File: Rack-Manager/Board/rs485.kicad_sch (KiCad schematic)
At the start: 28 parts, among them J5 Conn_01x03_Pin, J6 Conn_01x03_Pin, U8 THVD1450DRBR, U9 THVD1450DRBR

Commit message: Updated .gitignore, added USB-C sink controller and fix earth on GDT
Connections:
- net GND: no longer GD1.2, GD2.2
- new net Earth: GD1.2, GD2.2
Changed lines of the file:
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@@
+	)
+	(symbol
+		(lib_id "power:Earth")
+		(at 215.9 128.27 90)
+		(unit 1)
+		(exclude_from_sim no)
+		(in_bom yes)
+		(on_board yes)
+		(dnp no)
+		(property "Reference" "#PWR064"
+			(at 222.25 128.27 0)
+			(effects
+				(font
+					(size 1.27 1.27)
+				)
+				(hide yes)
+			)
+		)
+		(property "Value" "Earth"
+			(at 220.345 128.27 0)
+			(effects
+				(font
+					(size 1.27 1.27)
+				)
+			)
+		)
+		(property "Footprint" ""
+			(at 215.9 128.27 0)
+			(effects
+				(font
+					(size 1.27 1.27)
+				)
+				(hide yes)
+			)
+		)
+		(property "Datasheet" "~"
+			(at 215.9 128.27 0)
+			(effects
+				(font
+					(size 1.27 1.27)
+				)
+				(hide yes)
+			)
+		)
+		(property "Description" "Power symbol creates a global label with name \"Earth\""
+			(at 215.9 128.27 0)
+			(effects
+				(font
+					(size 1.27 1.27)
+				)
+				(hide yes)
+			)
+		)
+		(pin "1"
+		)
+		(instances
+			(project "Rack-Manager"
+				(path "/5d42174d-da49-4bca-870b-353868af7168/9f35d409-1fd7-4241-ba93-dffedac70e6f"
+					(reference "#PWR064")
+					(unit 1)
+				)
+			)
+		)
 	)
 	(symbol
@@
 	)
 	(symbol
-		(lib_id "power:GND")
+		(lib_id "power:Earth")
 		(at 215.9 55.88 90)
 		(unit 1)
@@
 		(on_board yes)
 		(dnp no)
-		(property "Reference" "#PWR045"
+		(property "Reference" "#PWR051"
 			(at 222.25 55.88 0)
 			(effects
@@
 			)
 		)
-		(property "Value" "GND"
-			(at 220.98 56.642 90)
+		(property "Value" "Earth"
+			(at 220.345 55.88 0)
 			(effects
 				(font
@@
 			)
 		)
-		(property "Datasheet" ""
+		(property "Datasheet" "~"
 			(at 215.9 55.88 0)
 			(effects
@@
 			)
 		)
-		(property "Description" "Power symbol creates a global label with name \"GND\" , ground"
+		(property "Description" "Power symbol creates a global label with name \"Earth\""
 			(at 215.9 55.88 0)
 			(effects
@@
 			(project "Rack-Manager"
 				(path "/5d42174d-da49-4bca-870b-353868af7168/9f35d409-1fd7-4241-ba93-dffedac70e6f"
-					(reference "#PWR045")
+					(reference "#PWR051")
 					(unit 1)
 				)
@@
 				(path "/5d42174d-da49-4bca-870b-353868af7168/9f35d409-1fd7-4241-ba93-dffedac70e6f"
 					(reference "#PWR070")
-					(unit 1)
-				)
-			)
-		)
-	)
-	(symbol
-		(lib_id "power:GND")
-		(at 195.58 128.27 90)
-		(unit 1)
-		(exclude_from_sim no)
-		(in_bom yes)
-		(on_board yes)
-		(dnp no)
-		(property "Reference" "#PWR039"
-			(at 201.93 128.27 0)
-			(effects
-				(font
-					(size 1.27 1.27)
-				)
-				(hide yes)
-			)
-		)
-		(property "Value" "GND"
-			(at 200.66 128.27 90)
-			(effects
-				(font
-					(size 1.27 1.27)
-				)
-			)
-		)
-		(property "Footprint" ""
-			(at 195.58 128.27 0)
-			(effects
-				(font
-					(size 1.27 1.27)
-				)
-				(hide yes)
-			)
-		)
-		(property "Datasheet" ""
-			(at 195.58 128.27 0)
-			(effects
-				(font
-					(size 1.27 1.27)
-				)
-				(hide yes)
-			)
-		)
-		(property "Description" "Power symbol creates a global label with name \"GND\" , ground"
-			(at 195.58 128.27 0)
-			(effects
-				(font
-					(size 1.27 1.27)
-				)
-				(hide yes)
-			)
-		)
-		(pin "1"
-		)
-		(instances
-			(project "Rack-Manager"
-				(path "/5d42174d-da49-4bca-870b-353868af7168/9f35d409-1fd7-4241-ba93-dffedac70e6f"
-					(reference "#PWR039")
 					(unit 1)
 				)
@@
 	)
 	(symbol
+		(lib_id "power:GND")
+		(at 195.58 55.88 90)
+		(unit 1)
+		(exclude_from_sim no)
+		(in_bom yes)
+		(on_board yes)
+		(dnp no)
+		(property "Reference" "#PWR045"
+			(at 201.93 55.88 0)
+			(effects
+				(font
+					(size 1.27 1.27)
+				)
+				(hide yes)
+			)
+		)
+		(property "Value" "GND"
+			(at 200.025 55.88 0)
+			(effects
+				(font
+					(size 1.27 1.27)
+				)
+			)
+		)
+		(property "Footprint" ""
+			(at 195.58 55.88 0)
+			(effects
+				(font
+					(size 1.27 1.27)
+				)
+				(hide yes)
+			)
+		)
+		(property "Datasheet" ""
+			(at 195.58 55.88 0)
+			(effects
+				(font
+					(size 1.27 1.27)
+				)
+				(hide yes)
+			)
+		)
+		(property "Description" "Power symbol creates a global label with name \"GND\" , ground"
+			(at 195.58 55.88 0)
+			(effects
+				(font
+					(size 1.27 1.27)
+				)
+				(hide yes)
+			)
+		)
+		(pin "1"
+		)
+		(instances
+			(project "Rack-Manager"
+				(path "/5d42174d-da49-4bca-870b-353868af7168/9f35d409-1fd7-4241-ba93-dffedac70e6f"
+					(reference "#PWR045")
+					(unit 1)
+				)
+			)
+		)
+	)
+	(symbol
 		(lib_id "Bourns:TBU-CA")
 		(at 196.85 39.37 0)
@@
 	)
 	(symbol
+		(lib_id "power:GND")
+		(at 195.58 128.27 90)
+		(unit 1)
+		(exclude_from_sim no)
+		(in_bom yes)
+		(on_board yes)
+		(dnp no)
+		(property "Reference" "#PWR039"
+			(at 201.93 128.27 0)
+			(effects
+				(font
+					(size 1.27 1.27)
+				)
+				(hide yes)
+			)
+		)
+		(property "Value" "GND"
+			(at 200.025 128.27 0)
+			(effects
+				(font
+					(size 1.27 1.27)
+				)
+			)
+		)
+		(property "Footprint" ""
+			(at 195.58 128.27 0)
+			(effects
+				(font
+					(size 1.27 1.27)
+				)
+				(hide yes)
+			)
+		)
+		(property "Datasheet" ""
+			(at 195.58 128.27 0)
+			(effects
+				(font
+					(size 1.27 1.27)
+				)
+				(hide yes)
+			)
+		)
+		(property "Description" "Power symbol creates a global label with name \"GND\" , ground"
+			(at 195.58 128.27 0)
+			(effects
+				(font
+					(size 1.27 1.27)
+				)
+				(hide yes)
+			)
+		)
+		(pin "1"
+		)
+		(instances
+			(project "Rack-Manager"
+				(path "/5d42174d-da49-4bca-870b-353868af7168/9f35d409-1fd7-4241-ba93-dffedac70e6f"
+					(reference "#PWR039")
+					(unit 1)
+				)
+			)
+		)
+	)
+	(symbol
 		(lib_id "Texas Instruments:THVD1450DRBR")
 		(at 127 119.38 0)
@@
 	)
 	(symbol
-		(lib_id "power:GND")
-		(at 195.58 55.88 90)
-		(unit 1)
-		(exclude_from_sim no)
-		(in_bom yes)
-		(on_board yes)
-		(dnp no)
-		(property "Reference" "#PWR051"
-			(at 201.93 55.88 0)
-			(effects
-				(font
-					(size 1.27 1.27)
-				)
-				(hide yes)
-			)
-		)
-		(property "Value" "GND"
-			(at 200.66 55.88 90)
-			(effects
-				(font
-					(size 1.27 1.27)
-				)
-			)
-		)
-		(property "Footprint" ""
-			(at 195.58 55.88 0)
-			(effects
-				(font
-					(size 1.27 1.27)
-				)
-				(hide yes)
-			)
-		)
-		(property "Datasheet" ""
-			(at 195.58 55.88 0)
-			(effects
-				(font
-					(size 1.27 1.27)
-				)
-				(hide yes)
-			)
-		)
-		(property "Description" "Power symbol creates a global label with name \"GND\" , ground"
-			(at 195.58 55.88 0)
-			(effects
-				(font
-					(size 1.27 1.27)
-				)
-				(hide yes)
-			)
-		)
-		(pin "1"
-		)
-		(instances
-			(project "Rack-Manager"
-				(path "/5d42174d-da49-4bca-870b-353868af7168/9f35d409-1fd7-4241-ba93-dffedac70e6f"
-					(reference "#PWR051")
-					(unit 1)
-				)
-			)
-		)
-	)
-	(symbol
 		(lib_id "Device:R_Small_US")
 		(at 167.64 62.23 90)
@@
 					(unit 1)
 				)
-			)
-		)
-	)
-	(symbol
-		(lib_id "power:GND")
-		(at 215.9 128.27 90)
-		(unit 1)
-		(exclude_from_sim no)
-		(in_bom yes)
-		(on_board yes)
-		(dnp no)
-		(property "Reference" "#PWR064"
-			(at 222.25 128.27 0)
-			(effects
-				(font
-					(size 1.27 1.27)
-				)
-				(hide yes)
-			)
-		)
-		(property "Value" "GND"
-			(at 220.98 129.032 90)
-			(effects
-				(font
-					(size 1.27 1.27)
-				)
-			)
-		)
-		(property "Footprint" ""
-			(at 215.9 128.27 0)
-			(effects
-				(font
-					(size 1.27 1.27)
-				)
-				(hide yes)
-			)
-		)
-		(property "Datasheet" ""
-			(at 215.9 128.27 0)
-			(effects
-				(font
-					(size 1.27 1.27)
-				)
-				(hide yes)
-			)
-		)
-		(property "Description" "Power symbol creates a global label with name \"GND\" , ground"
-			(at 215.9 128.27 0)
-			(effects
-				(font
-					(size 1.27 1.27)
-				)
-				(hide yes)
-			)
-		)
-		(pin "1"
-		)
-		(instances
-			(project "Rack-Manager"
-				(path "/5d42174d-da49-4bca-870b-353868af7168/9f35d409-1fd7-4241-ba93-dffedac70e6f"
-					(reference "#PWR064")
-					(unit 1)
-				)

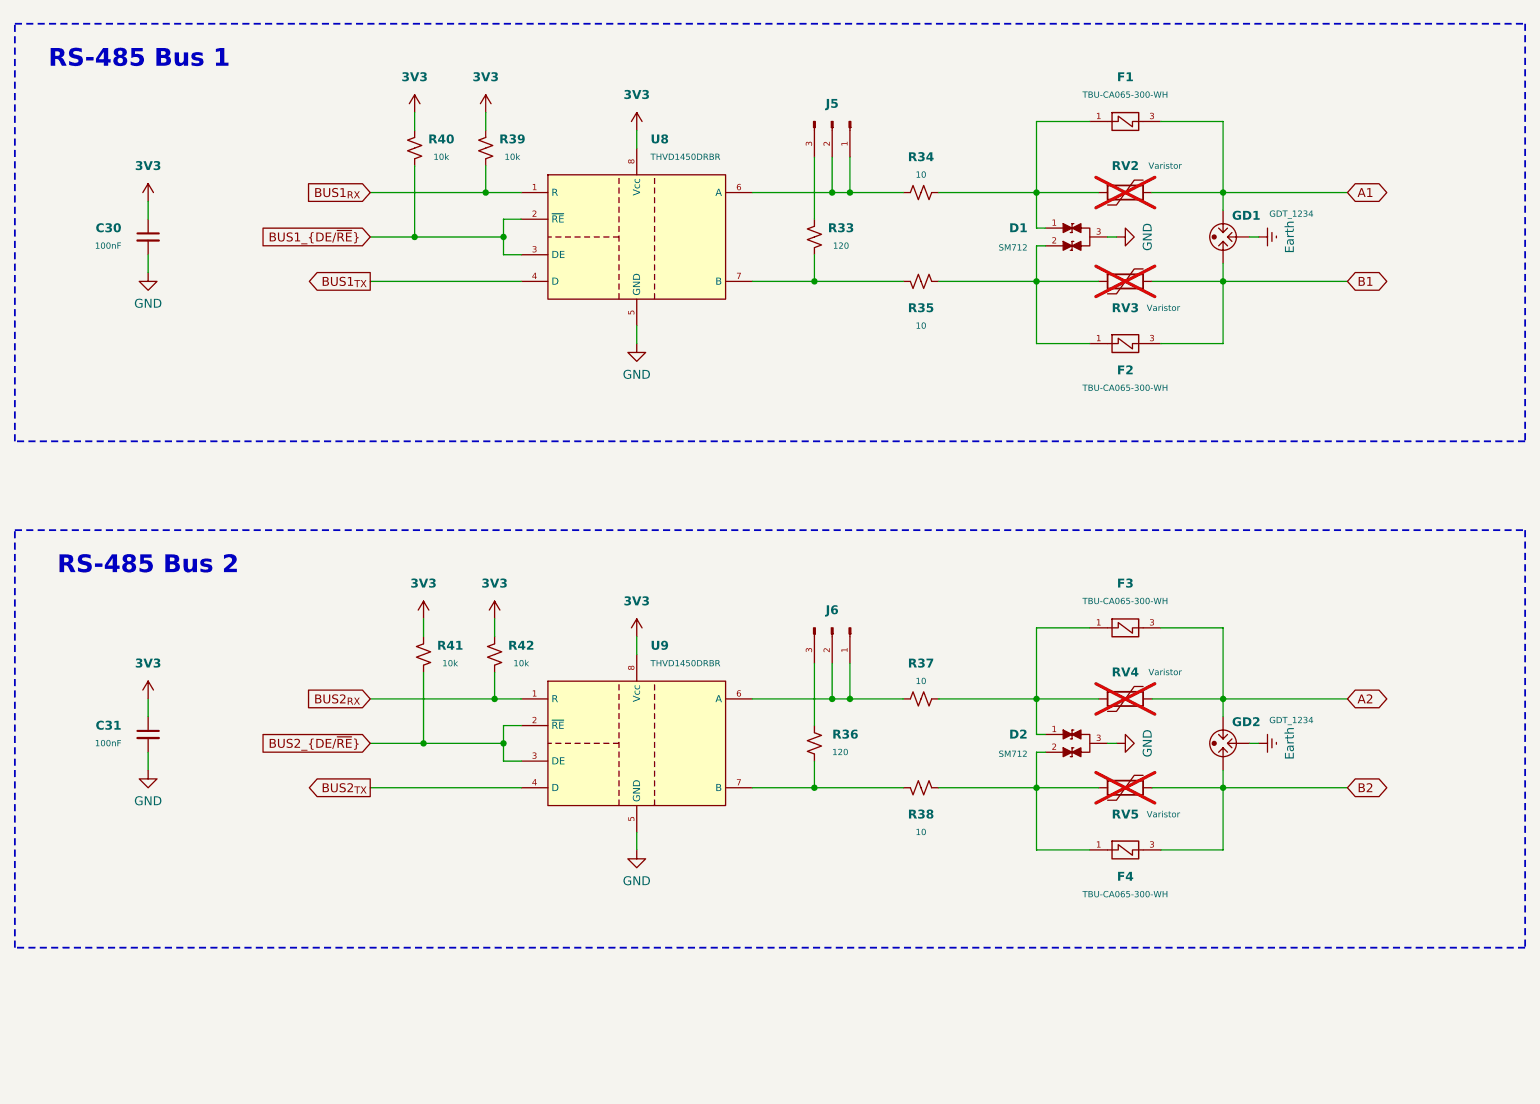
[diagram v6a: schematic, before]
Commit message: Added RS485 protection data as task describe and fixed stuff around
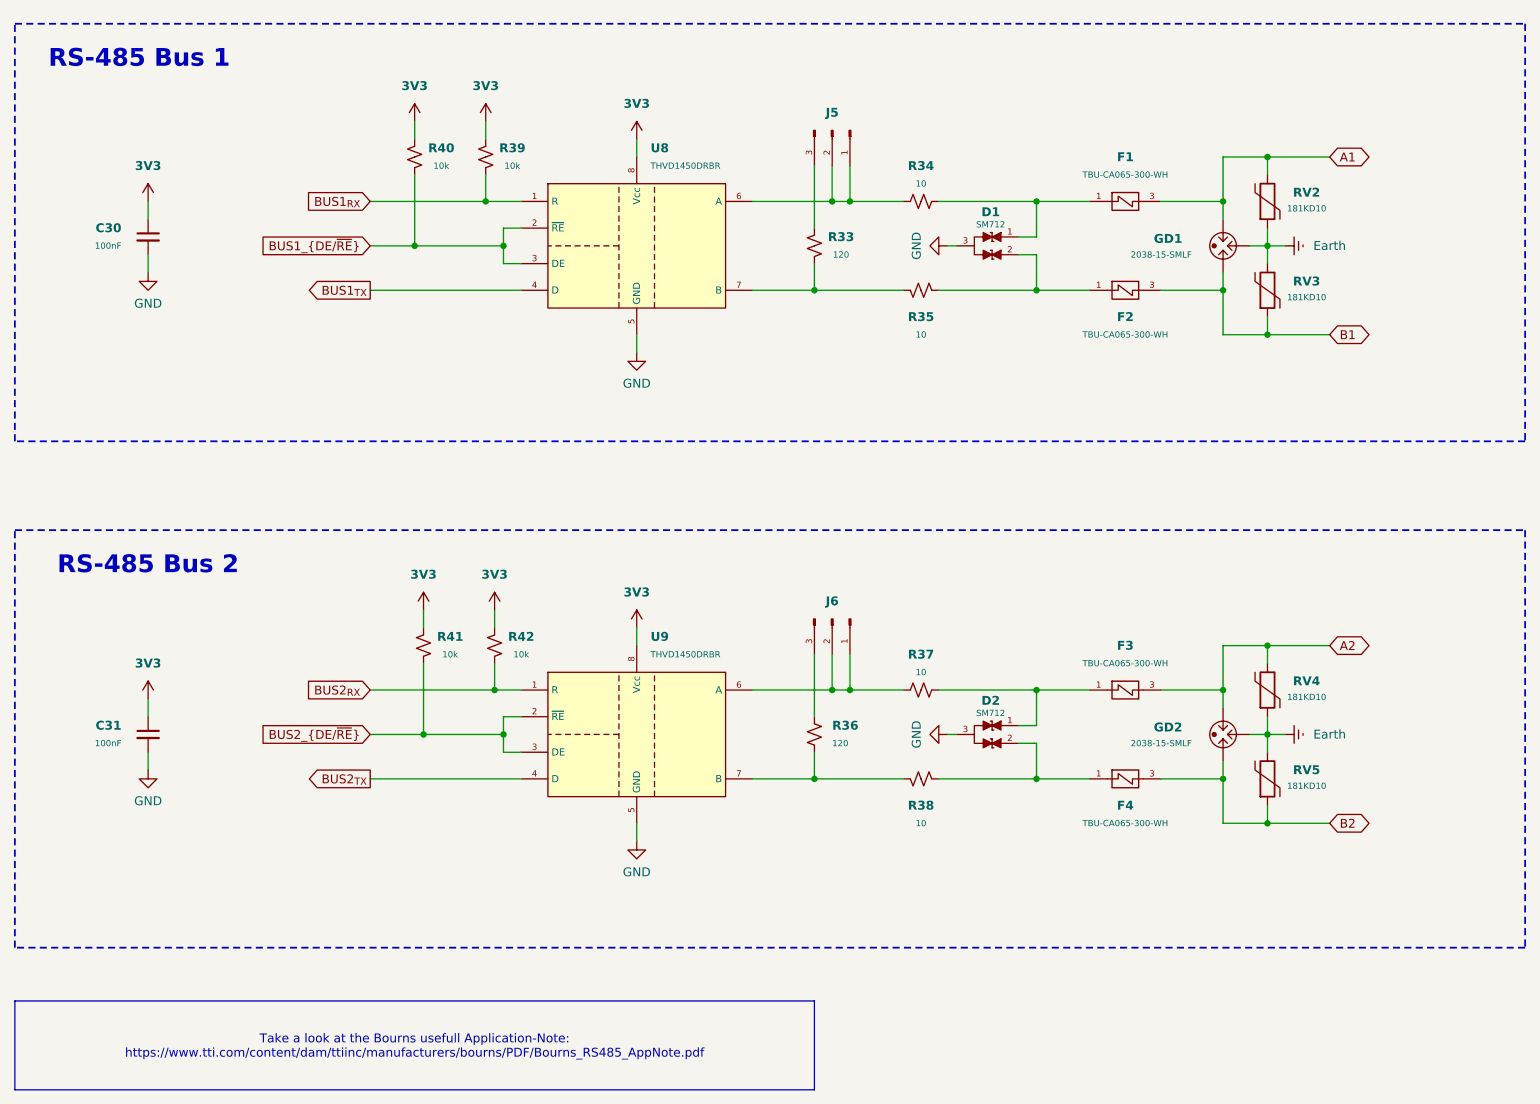
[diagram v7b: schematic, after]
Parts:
- GD1, GD2: value GDT_1234 -> 2038-15-SMLF; footprint (none) -> Fuse:GDT_Bourns_2038
- RV2, RV3, RV4, RV5: value Varistor -> 181KD10; footprint (none) -> Varistor:RV_Disc_D12mm_W4.5mm_P7.5mm; now fitted
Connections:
- net B1: now also RV3.2; no longer RV3.1
- net B2: now also RV5.2; no longer RV5.1
- net Earth: now also RV2.2, RV3.1, RV4.2, RV5.1
- net at D2.2 (A2), F4.1, R38.2: no longer RV5.2
- net at D1.1 (A1), F1.1, R34.2: no longer RV2.2
- net at D2.1 (A1), F3.1, R37.2: no longer RV4.2
- net at D1.2 (A2), F2.1, R35.2: no longer RV3.2
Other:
- moved on the sheet: D1, F1, F2, GD1, J5, J6, R33, R34, R35, R36, R37, R38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
